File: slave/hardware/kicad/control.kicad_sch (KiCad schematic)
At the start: 24 parts, among them IC5 STM32G431C8T6TR, SW1 SW_Push, SW2 SW_Push, Y1 8Mhz

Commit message: feat(HW): add digital input circuit files
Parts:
- renumbered C24 to C20, C23 to C21, C21 to C23, C32 to C24, C20 to C25, C28 to C26, C29 to C27, C33 to C28, C25 to C29, C26 to C31, C31 to C32, C27 to C33, R5 to R8, R6 to R9, TP9 to TP7, TP7 to TP9
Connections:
- net at IC5.37 (PA13): no longer IC5.38 (PA14)

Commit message: refactor(HW): reduce analog inputs and update MCU analog connections
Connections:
- net ADC1_OUT2: now reaches IC5.10 (PA2)
- net ADC1_OUT3: now reaches IC5.11 (PA3)
- net ADC2_OUT0: now reaches IC5.13 (PA5)
- net ADC1_OUT1: now reaches IC5.14 (PA6)
- net ADC1_OUT1: now also IC5.9 (PA1)
- net ADC0_OUT2: now reaches IC5.15 (PA7)
- net ADC2_OUT3: now reaches IC5.18 (PB2)
- net ADC1_OUT0: now reaches IC5.8 (PA0)
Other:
- moved on the sheet: IC5A

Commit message: refactor(HW): rename components and fix reference designators
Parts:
- renumbered C20 to C36, C21 to C37, C22 to C38, C23 to C39, C24 to C40, C25 to C41, C26 to C42, C27 to C43, C28 to C44, C29 to C45, C30 to C46, C31 to C47, C32 to C48, C33 to C49, IC5 to IC9, R8 to R40, R9 to R41, TP7 to TP23, TP8 to TP24, TP9 to TP25
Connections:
- net VBUS: now reaches IC9.31 (PA9)

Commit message: feat(HW): add footprints and configure component properties
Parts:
- IC9: footprint QFP50P900X900X160-48N -> Datalogger:QFP50P900X900X160-48N
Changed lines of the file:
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@@
 			)
 		)
-		(property "Footprint" "QFP50P900X900X160-48N"
+		(property "Footprint" "Datalogger:QFP50P900X900X160-48N"
 			(at 216.154 106.426 0)
 			(hide yes)
@@
 			)
 		)
-		(property "Footprint" "QFP50P900X900X160-48N"
+		(property "Footprint" "Datalogger:QFP50P900X900X160-48N"
 			(at 82.804 105.156 0)
 			(hide yes)

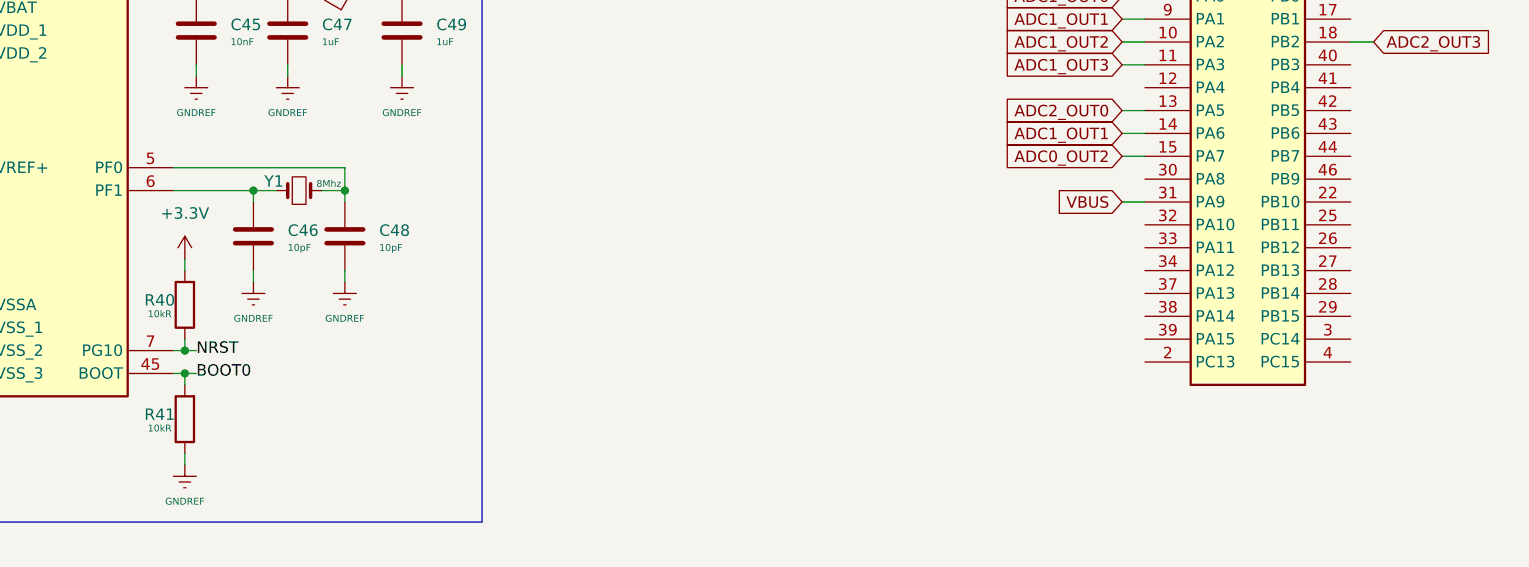
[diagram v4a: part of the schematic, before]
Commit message: feat(HW): add MCU connections
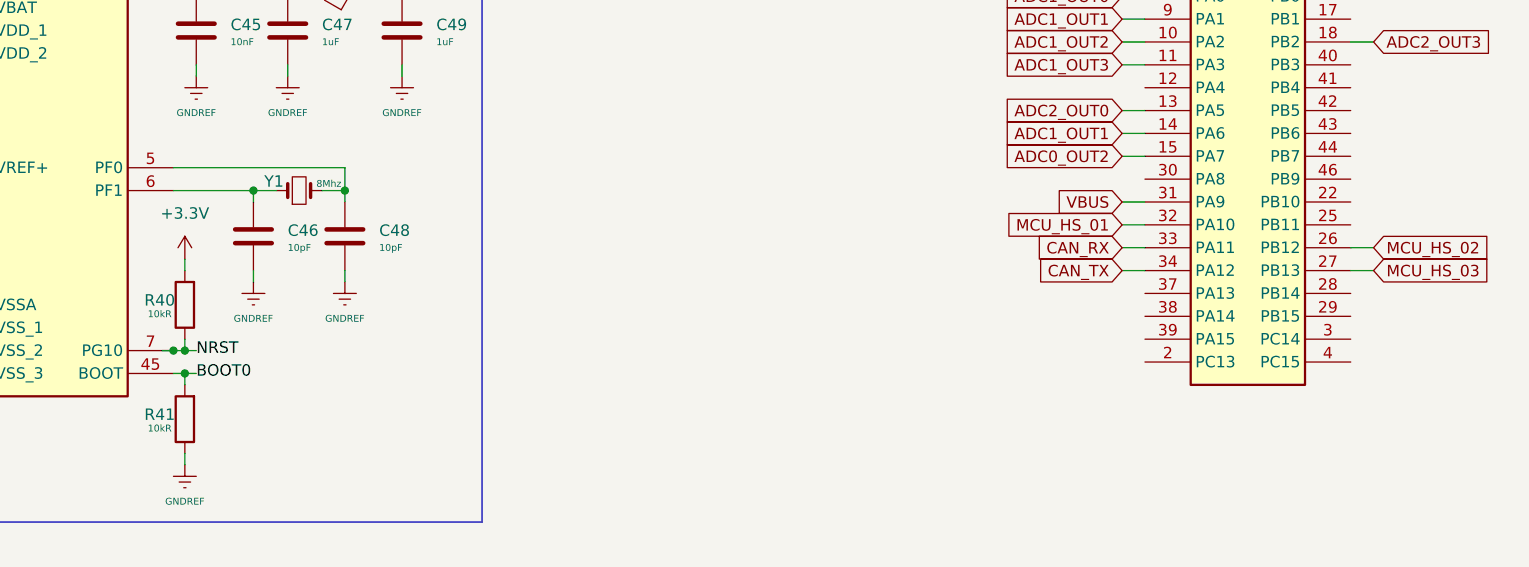
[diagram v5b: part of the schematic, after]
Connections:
- net MCU_HS_02: now reaches IC9.26 (PB12)
- net MCU_HS_03: now reaches IC9.27 (PB13)
- net MCU_HS_01: now reaches IC9.32 (PA10)
- net CAN_RX: now reaches IC9.33 (PA11)
- net CAN_TX: now reaches IC9.34 (PA12)
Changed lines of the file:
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@@
+	)
+	(junction
+		(at 105.41 92.71)
+		(diameter 0)
+		(color 0 0 0 0)
 	)
 	(junction
@@
 	(wire
 		(pts
+			(xy 210.82 81.28) (xy 213.36 81.28)
+		)
+		(stroke
+			(width 0)
+			(type default)
+			(color 255 106 0 1)
+		)
+	)
+	(wire
+		(pts
 			(xy 114.3 74.93) (xy 114.3 76.2)
 		)
@@
 			(width 0)
 			(type default)
+			(color 255 106 0 1)
 		)
 	)
@@
 	(wire
 		(pts
+			(xy 210.82 83.82) (xy 213.36 83.82)
+		)
+		(stroke
+			(width 0)
+			(type default)
+			(color 255 106 0 1)
+		)
+	)
+	(wire
+		(pts
 			(xy 78.74 90.17) (xy 80.01 90.17)
 		)
@@
 	(wire
 		(pts
+			(xy 236.22 81.28) (xy 238.76 81.28)
+		)
+		(stroke
+			(width 0)
+			(type default)
+			(color 255 106 0 1)
+		)
+	)
+	(wire
+		(pts
 			(xy 114.3 83.82) (xy 114.3 85.09)
 		)
@@
 	(wire
 		(pts
+			(xy 104.14 92.71) (xy 105.41 92.71)
+		)
+		(stroke
+			(width 0)
+			(type default)
+		)
+	)
+	(wire
+		(pts
 			(xy 210.82 55.88) (xy 213.36 55.88)
 		)
@@
 	(wire
 		(pts
+			(xy 210.82 78.74) (xy 213.36 78.74)
+		)
+		(stroke
+			(width 0)
+			(type default)
+			(color 255 106 0 1)
+		)
+	)
+	(wire
+		(pts
 			(xy 49.53 52.07) (xy 59.69 52.07)
 		)
@@
 		(pts
 			(xy 29.21 46.99) (xy 29.21 52.07)
+		)
+		(stroke
+			(width 0)
+			(type default)
+			(color 255 106 0 1)
+		)
+	)
+	(wire
+		(pts
+			(xy 236.22 83.82) (xy 238.76 83.82)
 		)
 		(stroke
@@
 		)
 	)
+	(global_label "CAN_RX"
+		(shape input)
+		(at 210.82 81.28 180)
+		(fields_autoplaced yes)
+		(effects
+			(font
+				(size 1.27 1.27)
+				(thickness 0.1111)
+			)
+			(justify right)
+		)
+		(property "Intersheetrefs" "${INTERSHEET_REFS}"
+			(at 200.9371 81.28 0)
+			(hide yes)
+			(show_name no)
+			(do_not_autoplace no)
+			(effects
+				(font
+					(size 1.27 1.27)
+				)
+				(justify right)
+			)
+		)
+	)
 	(global_label "ADC1_OUT3"
 		(shape input)
@@
 		)
 	)
+	(global_label "MCU_HS_03"
+		(shape input)
+		(at 238.76 83.82 0)
+		(fields_autoplaced yes)
+		(effects
+			(font
+				(size 1.27 1.27)
+			)
+			(justify left)
+		)
+		(property "Intersheetrefs" "${INTERSHEET_REFS}"
+			(at 252.6913 83.82 0)
+			(hide yes)
+			(show_name no)
+			(do_not_autoplace no)
+			(effects
+				(font
+					(size 1.27 1.27)
+				)
+				(justify left)
+			)
+		)
+	)
 	(global_label "ADC1_OUT1"
 		(shape input)
@@
 			)
 		)
+	)
+	(global_label "CAN_TX"
+		(shape input)
+		(at 210.82 83.82 180)
+		(fields_autoplaced yes)
+		(effects
+			(font
+				(size 1.27 1.27)
+				(thickness 0.1111)
+			)
+			(justify right)
+		)
+		(property "Intersheetrefs" "${INTERSHEET_REFS}"
+			(at 201.2395 83.82 0)
+			(hide yes)
+			(show_name no)
+			(do_not_autoplace no)
+			(effects
+				(font
+					(size 1.27 1.27)
+				)
+				(justify right)
+			)
+		)
+	)
+	(global_label "MCU_HS_01"
+		(shape input)
+		(at 210.82 78.74 180)
+		(fields_autoplaced yes)
+		(effects
+			(font
+				(size 1.27 1.27)
+			)
+			(justify right)
+		)
+		(property "Intersheetrefs" "${INTERSHEET_REFS}"
+			(at 196.8887 78.74 0)
+			(hide yes)
+			(show_name no)
+			(do_not_autoplace no)
+			(effects
+				(font
+					(size 1.27 1.27)
+				)
+				(justify right)
+			)
+		)
+	)
+	(global_label "MCU_HS_02"
+		(shape input)
+		(at 238.76 81.28 0)
+		(fields_autoplaced yes)
+		(effects
+			(font
+				(size 1.27 1.27)
+			)
+			(justify left)
+		)
+		(property "Intersheetrefs" "${INTERSHEET_REFS}"
+			(at 252.6913 81.28 0)
+			(hide yes)
+			(show_name no)
+			(do_not_autoplace no)
+			(effects
+				(font
+					(size 1.27 1.27)
+				)
+				(justify left)
+			)
+		)

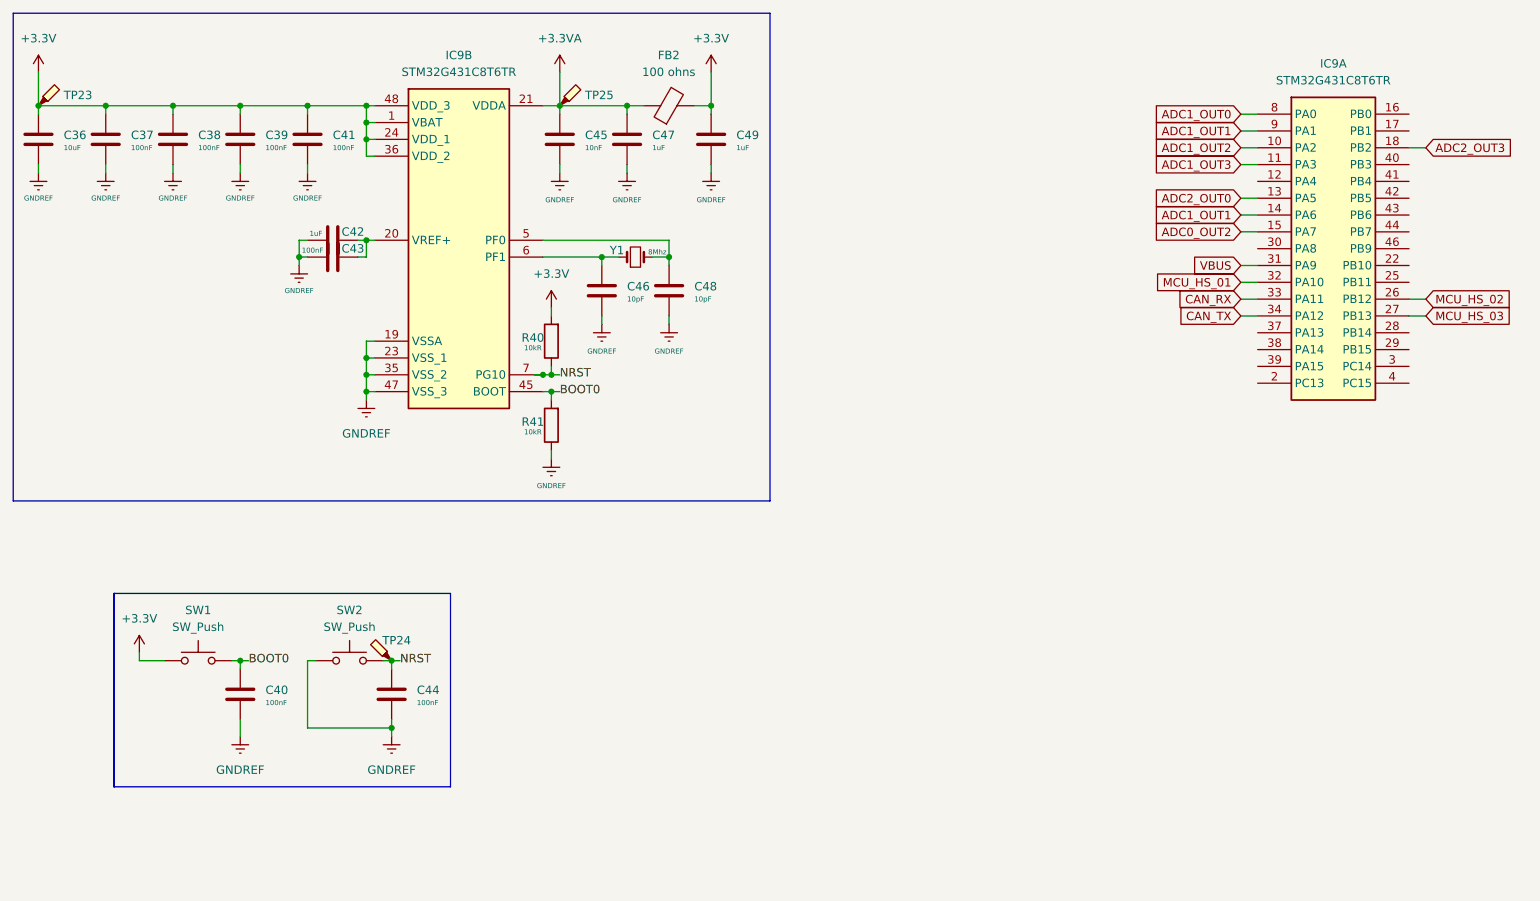
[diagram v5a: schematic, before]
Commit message: refactor(HW): finalize GPIO configuration
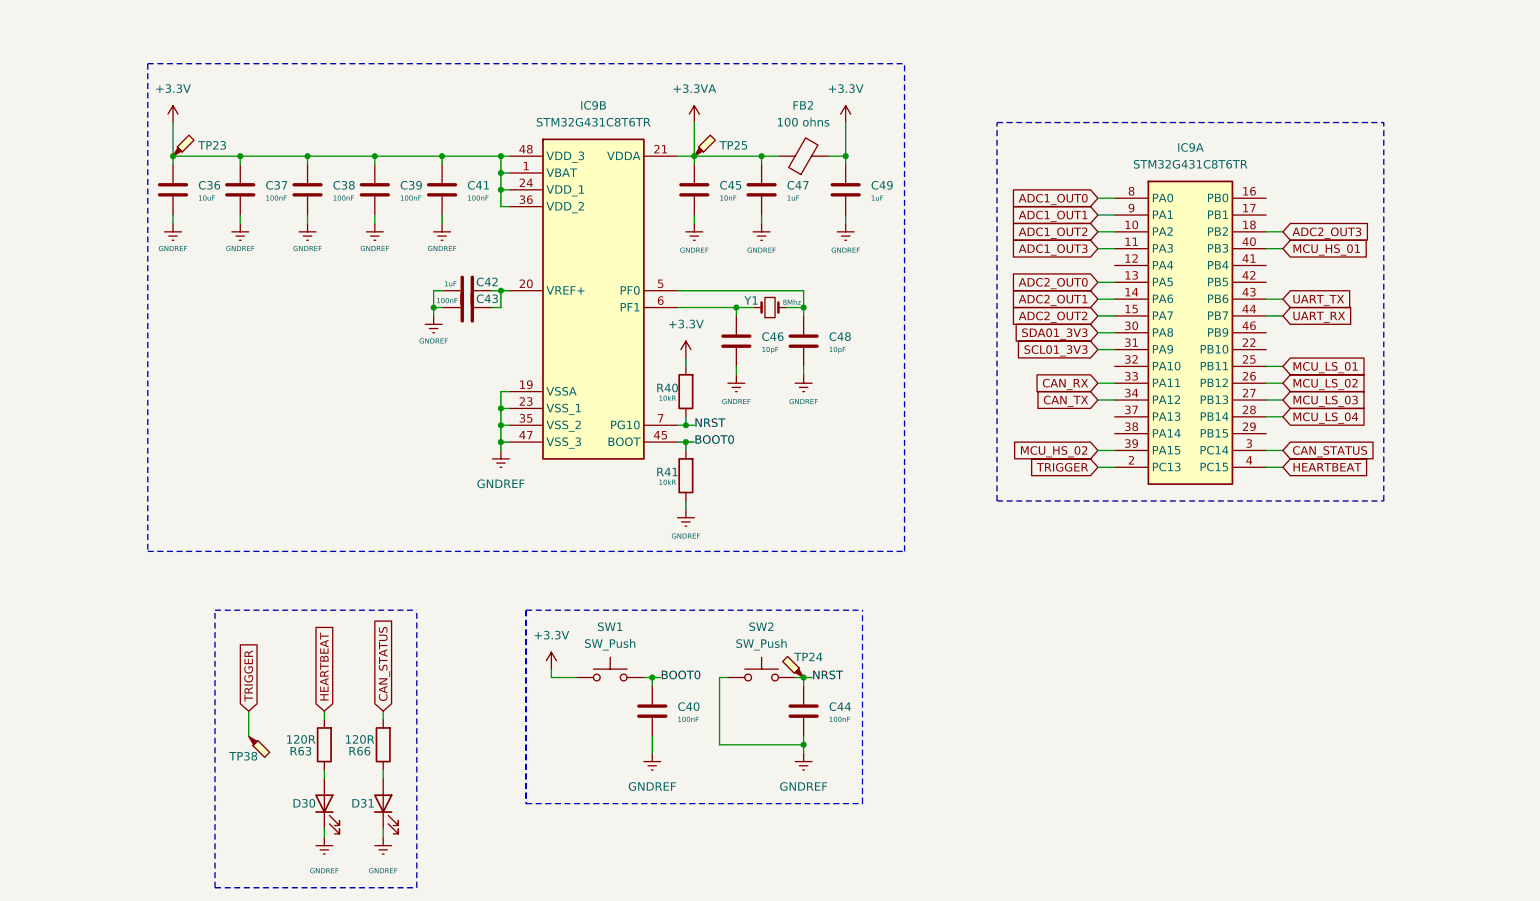
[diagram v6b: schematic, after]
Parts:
- added D30, D31: LED, LED_SMD:LED_01005_0402Metric, symbol Device:LED
- added R63, R66: 120R, Resistor_SMD:R_0805_2012Metric, symbol Device:R
- added TP38: (no value), TestPoint:TestPoint_Pad_2.0x2.0mm, symbol Connector:TestPoint_Probe
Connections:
- net ADC1_OUT1: no longer IC9.14 (PA6)
- net GNDREF: now also D30.1 (K), D31.1 (K)
- net MCU_HS_01: now also IC9.40 (PB3); no longer IC9.32 (PA10)
- net MCU_HS_02: now also IC9.39 (PA15); no longer IC9.26 (PB12)
- net TRIGGER: now reaches IC9.2 (PC13)
- net TRIGGER: now also TP38.1
- net MCU_LS_01: now reaches IC9.25 (PB11)
- net MCU_LS_04: now reaches IC9.28 (PB14)
- net CAN_STATUS: now reaches IC9.3 (PC14)
- net CAN_STATUS: now also R66.2
- net SDA01_3V3: now reaches IC9.30 (PA8)
- net HEARTBEAT: now reaches IC9.4 (PC15)
- net HEARTBEAT: now also R63.2
- net UART_TX: now reaches IC9.43 (PB6)
- net UART_RX: now reaches IC9.44 (PB7)
- net ADC0_OUT2 renamed ADC2_OUT2
- net MCU_HS_03 renamed MCU_LS_03
- net VBUS renamed SCL01_3V3
- new net: D31.2 (A), R66.1
- new net: D30.2 (A), R63.1
- new net ADC2_OUT1: IC9.14 (PA6)
- new net MCU_LS_02: IC9.26 (PB12)
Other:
- moved on the sheet: C36, C37, C38, C39, C40, C41, C42, C43, C44, C45, C46, C47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
